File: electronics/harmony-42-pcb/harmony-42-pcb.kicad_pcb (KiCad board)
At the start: 2 copper layers, 285.8 x 133.3 mm, 84 parts

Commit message: Add routes
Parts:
- moved SW37 42.3 mm to (225.6, 98.2), turned to -160.946 degrees
- moved SW39 42.3 mm to (188.4, 118.3), turned to -141.891 degrees
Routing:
- net Net-(SW18-Pad1): track 0.00 -> 2.40 mm, vias 0 -> 6
- net Net-(SW14-Pad1): vias 0 -> 1
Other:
- board size 285.8 x 133.3 mm -> 285.8 x 123.8 mm

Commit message: Add routes
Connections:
- D37 pad 2: Net-(D37-A) -> Net-(D39-A)
- D39 pad 2: Net-(D39-A) -> Net-(D37-A)
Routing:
- net Net-(SW17-Pad1): track 0.00 -> 3.60 mm, vias 0 -> 6
- net Net-(SW16-Pad1): track 0.00 -> 3.60 mm, vias 0 -> 6
- net Net-(SW15-Pad1): track 0.00 -> 2.40 mm, vias 0 -> 4
- net Net-(SW1-Pad1): track 0.00 -> 2.40 mm, vias 0 -> 4
- net Net-(SW14-Pad1): track 0.00 -> 2.40 mm, vias 1 -> 4
- net Net-(SW18-Pad1): track 2.40 -> 3.60 mm
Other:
- outline, holes or cut-outs redrawn

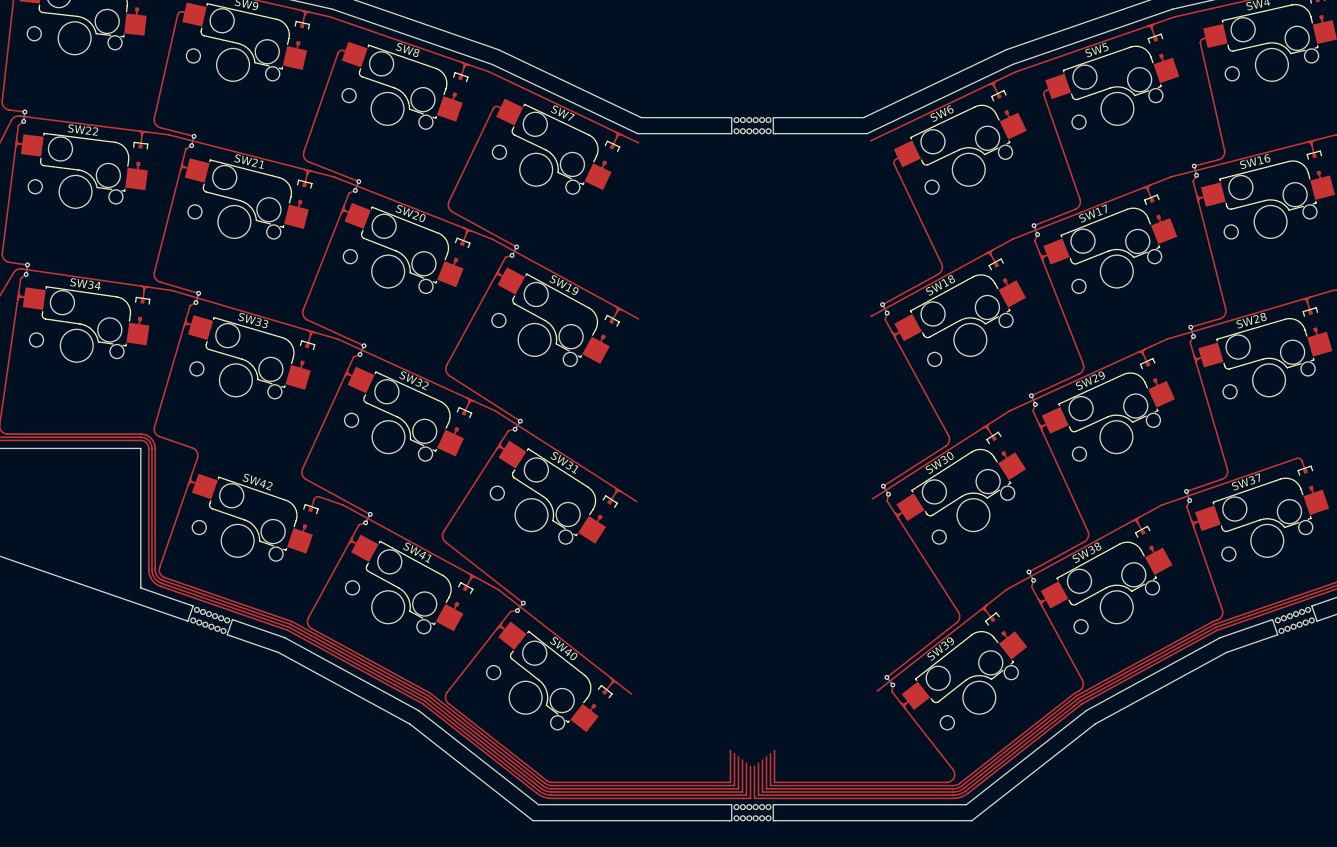
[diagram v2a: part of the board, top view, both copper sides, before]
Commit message: Add routes
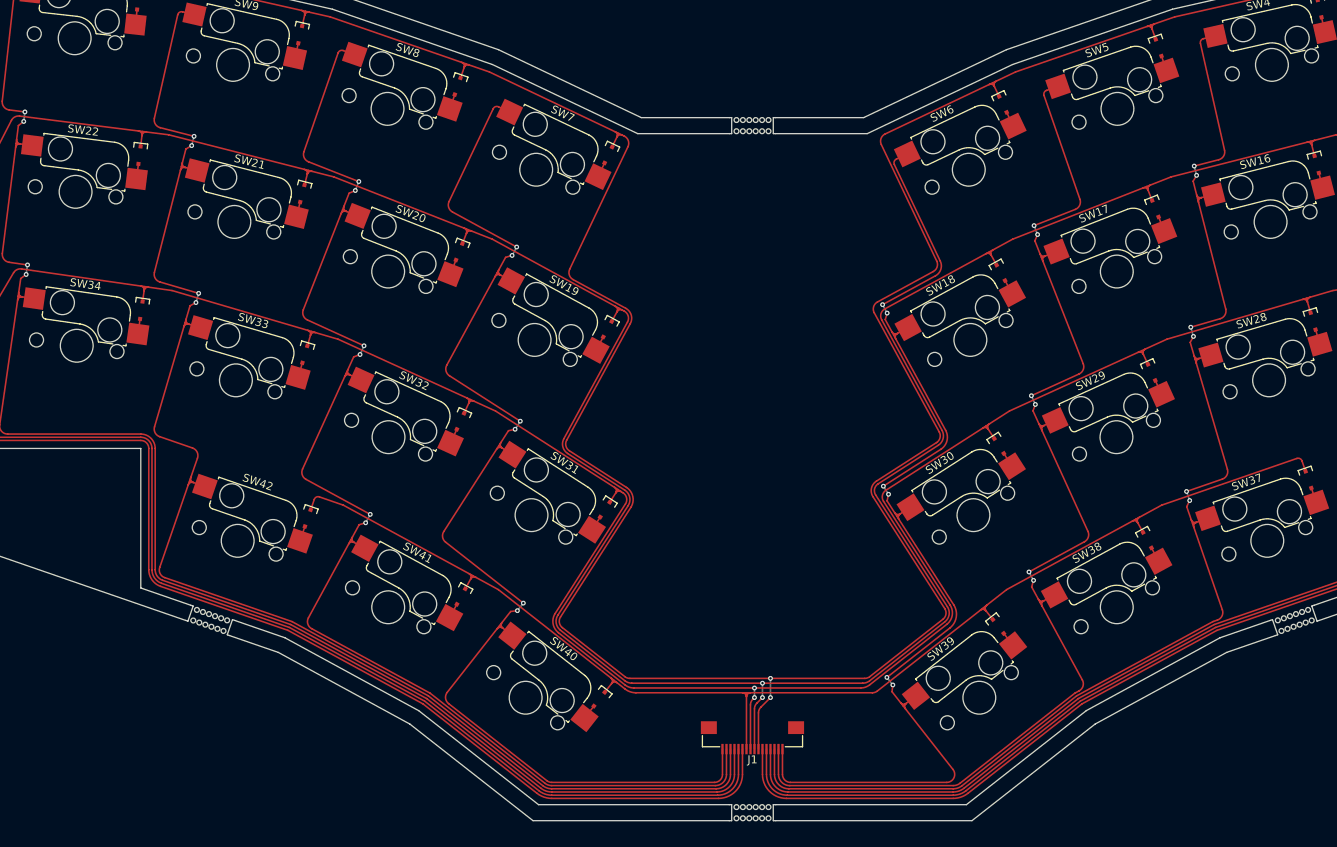
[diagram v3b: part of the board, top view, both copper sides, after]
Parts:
- added J1: FFC Connector, Project_Library:JUSHUO_AFC01-S16FCC-00, F.Cu at (161.9, 126.8)
- renumbered D39 to D37, D37 to D39
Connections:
- net Net-(D1-K) renamed ROW0
- net Net-(D13-K) renamed ROW1
- net Net-(D25-K) renamed ROW2
- net Net-(D37-K) renamed ROW3
- net Net-(SW1-Pad1) renamed COL0
- net Net-(SW10-Pad1) renamed COL9
- net Net-(SW11-Pad1) renamed COL10
- net Net-(SW12-Pad1) renamed COL11
- net Net-(SW14-Pad1) renamed COL1
- net Net-(SW15-Pad1) renamed COL2
- net Net-(SW16-Pad1) renamed COL3
- net Net-(SW17-Pad1) renamed COL4
- net Net-(SW18-Pad1) renamed COL5
- net Net-(SW19-Pad1) renamed COL6
- net Net-(SW20-Pad1) renamed COL7
- net Net-(SW21-Pad1) renamed COL8
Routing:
- net ROW0: track 0.00 -> 9.41 mm, vias 2 -> 4
- net ROW1: track 0.00 -> 8.61 mm, vias 0 -> 2
- net ROW2: track 0.00 -> 7.80 mm, vias 0 -> 2

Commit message: Change routes
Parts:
- moved J1 19.0 mm to (161.9, 107.8)
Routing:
- net ROW0: track 9.41 -> 0.00 mm, vias 4 -> 2
- net ROW1: track 8.61 -> 0.00 mm, vias 2 -> 0
- net ROW2: track 7.80 -> 0.00 mm, vias 2 -> 0
- net COL7: track 3.60 -> 2.40 mm
- net COL6: track 3.60 -> 2.40 mm
- net COL8: vias 4 -> 6
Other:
- outline, holes or cut-outs redrawn

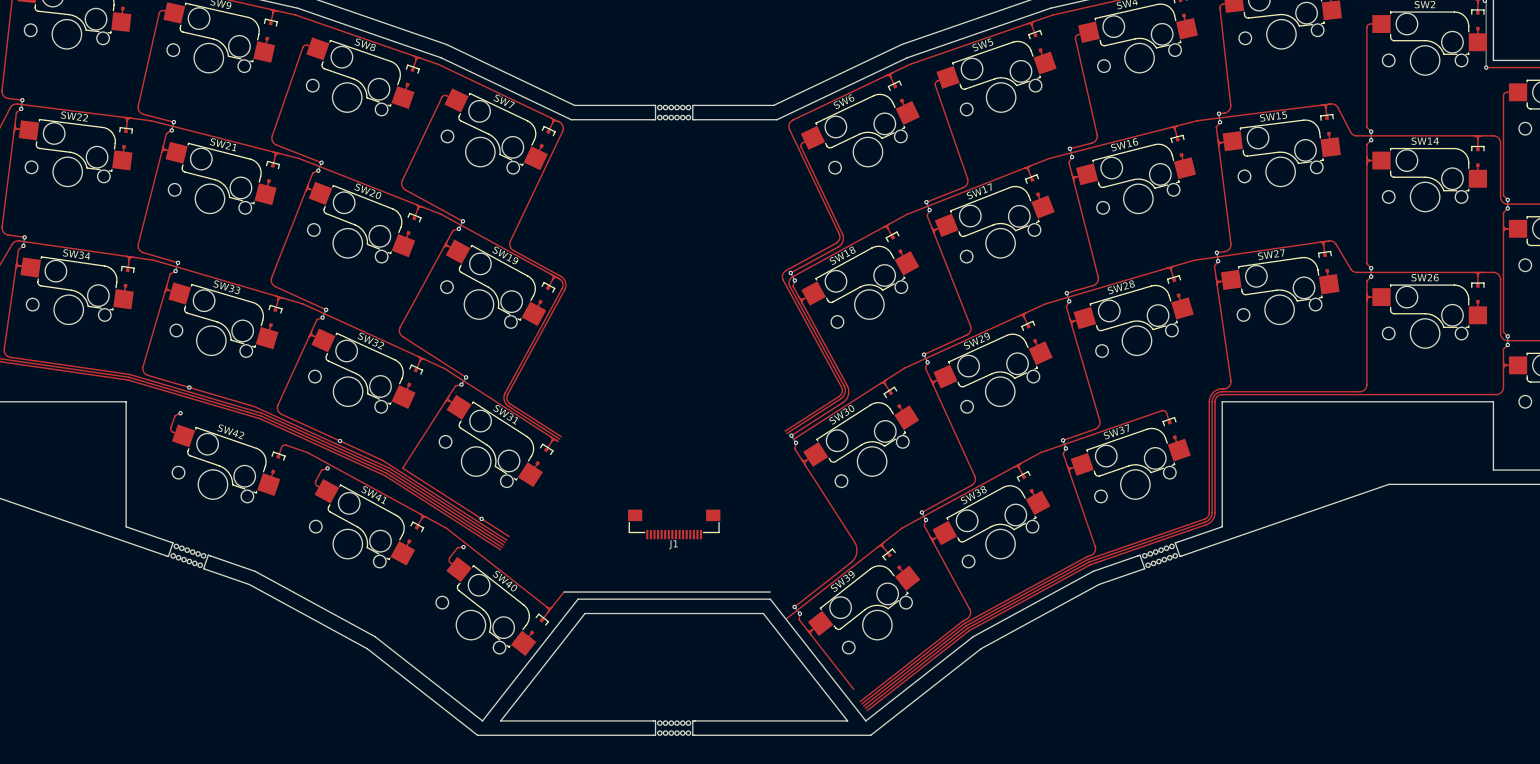
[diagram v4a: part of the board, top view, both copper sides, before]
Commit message: Add routes
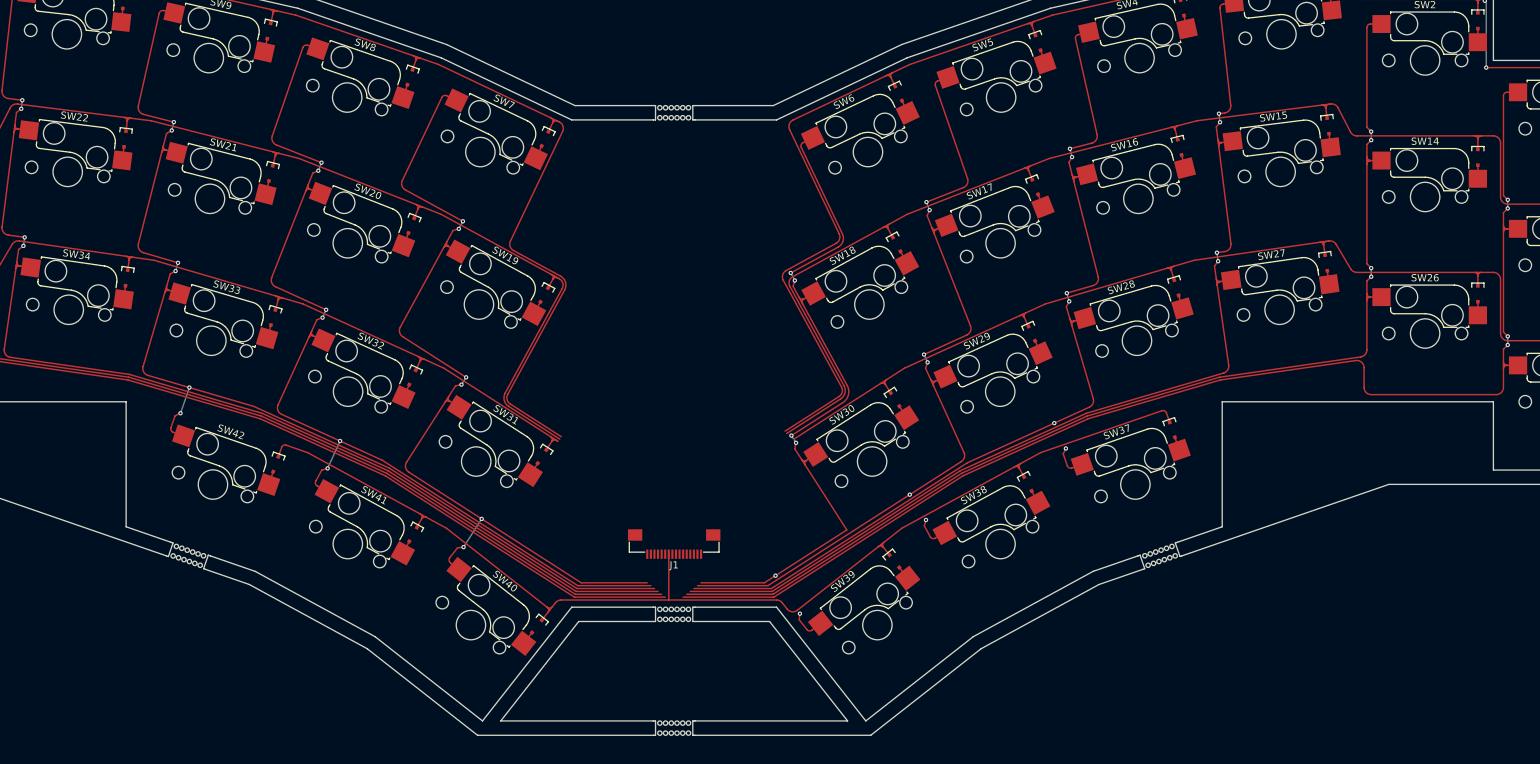
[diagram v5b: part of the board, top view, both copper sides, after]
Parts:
- moved J1 2.74 mm to (161.9, 110.5)
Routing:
- net COL6: track 2.40 -> 7.08 mm
- net COL7: track 2.40 -> 6.60 mm
- net COL8: track 2.40 -> 6.20 mm
- net COL3: track 3.60 -> 2.40 mm
- net COL5: track 3.60 -> 2.40 mm
- net COL4: track 3.60 -> 2.40 mm
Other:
- outline, holes or cut-outs redrawn

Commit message: Add routes
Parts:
- added REF**: Fiducial_1mm_Mask2mm, Fiducial:Fiducial_1mm_Mask2mm, F.Cu at (23.1, 138.9)
- added REF**: Fiducial_1mm_Mask2mm, Fiducial:Fiducial_1mm_Mask2mm, F.Cu at (23.1, 23.1)
- added REF**: Fiducial_1mm_Mask2mm, Fiducial:Fiducial_1mm_Mask2mm, F.Cu at (300.8, 23.1)
- added REF**: Fiducial_1mm_Mask2mm, Fiducial:Fiducial_1mm_Mask2mm, F.Cu at (300.8, 138.9)
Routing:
- net COL4: track 2.40 -> 6.60 mm
- net COL3: track 2.40 -> 6.28 mm
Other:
- outline, holes or cut-outs redrawn

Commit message: Add routes
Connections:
- J1 pad 1: COL5 -> ROW0
- J1 pad 2: COL4 -> ROW1
- J1 pad 3: COL3 -> ROW2
- J1 pad 4: COL2 -> COL5
- J1 pad 5: COL1 -> COL4
- J1 pad 6: COL0 -> COL3
- J1 pad 7: ROW0 -> COL2
- J1 pad 8: ROW1 -> COL1
- J1 pad 9: ROW2 -> COL0
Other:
- outline, holes or cut-outs redrawn

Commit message: Update pcb
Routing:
- added copper zone on B.Cu, net (none)
- added copper zone on F.Cu, net (none)
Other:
- outline, holes or cut-outs redrawn
- board text added: "1.0.0+20240705"
- board text added: "@takayoshiotake"
- board text added: "Harmony 42"
- board text added: "JLCJLCJLCJLC"
